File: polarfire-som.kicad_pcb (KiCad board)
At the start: 2 copper layers, 55 x 40 mm, 16 parts, among them J1 CM4_Plug_Module_Hirose_DF40_2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, J3 PinHeader_2x5_P1.27mm_SMD, U1 MPFS250T-FCVG484, U2 SDINBDG4-8G, U3 DP83867ISRGZR, U4 MT25QL01GBBB8E_SOP2-16, U5 PAC1934_QFN, U6 TPS65296, U7 MT53D512M32D2_WFBGA, U8 USB3300-EZK-TR, U9 CrossLink_LIF-MD6000-6JMG80I

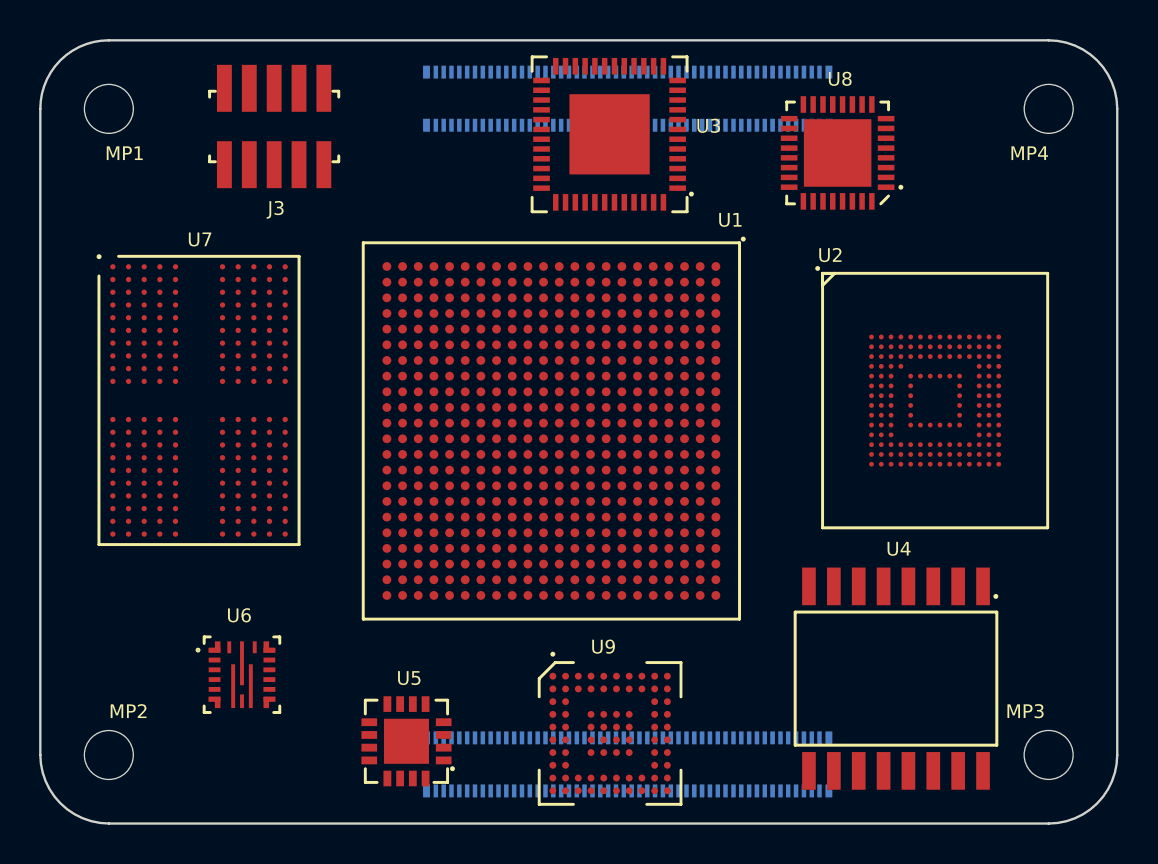
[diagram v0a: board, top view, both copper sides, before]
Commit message: [#52579] Add Antmicro and OSHW logo
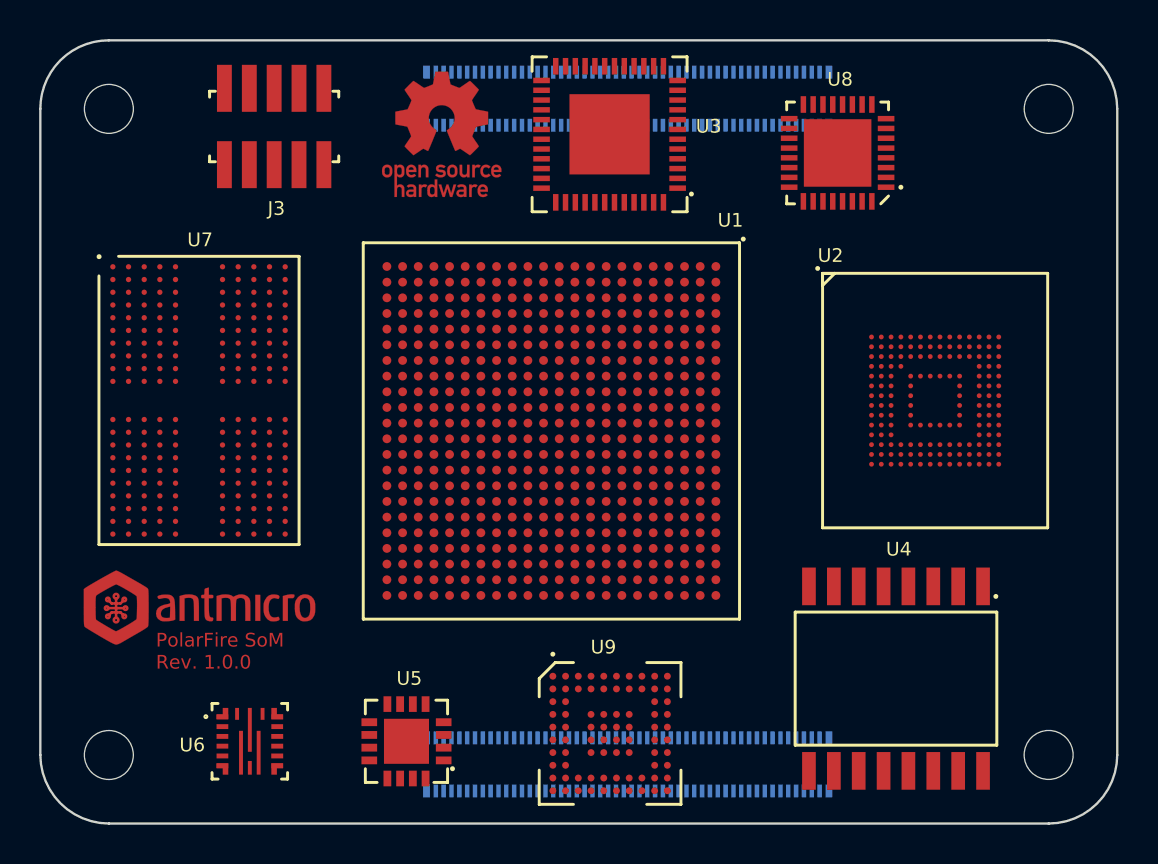
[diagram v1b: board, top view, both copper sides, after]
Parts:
- added N1: antmicro_logo, antmicro-footprints:antmicro-logo_scaled_12mm, F.Cu at (105.8, 71.4)
- added N2: oshw_logo, antmicro-footprints:oshw-logo, F.Cu at (118.2, 47.2)
- moved U6 3.42 mm to (108.4, 78.2)
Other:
- board text added: "PolarFire SoM Rev. 1.0.0"
